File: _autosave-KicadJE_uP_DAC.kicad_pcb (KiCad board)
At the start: 2 copper layers, 100 x 100 mm, 273 parts, among them J201 CV1, J202 CV2, J203 OUT1, J204 OUT2, J205 IN1, J206 IN2, J301 AVR-ISP-6, J302 UART, J401 CV1, J402 CV2, J403 OUT1, J404 OUT2, J405 OUT3, J406 OUT4, J407 IN1, J408 IN2, J409 I2C, J501 BOOT, J502 UART, J503 USB_B_Micro, J601 CV1, J602 FM_lin, J603 Sync, J604 PWM, J605 Ramp, J606 Tri, J607 Sine, J608 555_Pulse, P201 Doepfer_Power_16pin, P401 Doepfer_Power_16pin, P601 Doepfer_Power_16pin, SW201 SW_SPDT, SW401 SW_SPDT, U201 TL072, U202 MCP4822, U301 ATmega32A-AU, U401 TL072, U402 TL072, U405 MCP4822, U501 AMS1117-3.3, U502 STM32F103C8Tx, U601 TLC555, U602 TL074, U603 TL074, Y301 16MHz, Y501 8 MHz

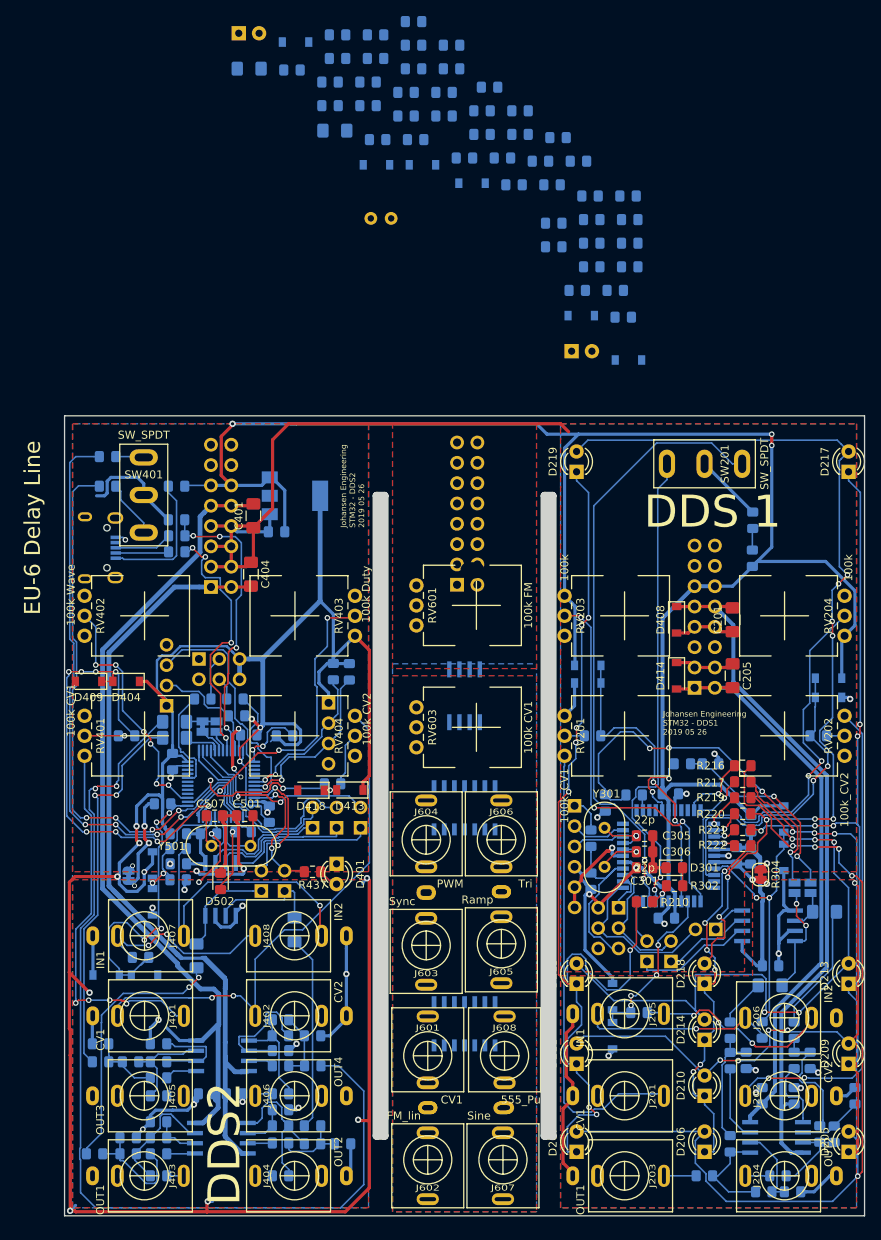
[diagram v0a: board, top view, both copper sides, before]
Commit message: 16p -> 10p on 555 VCO
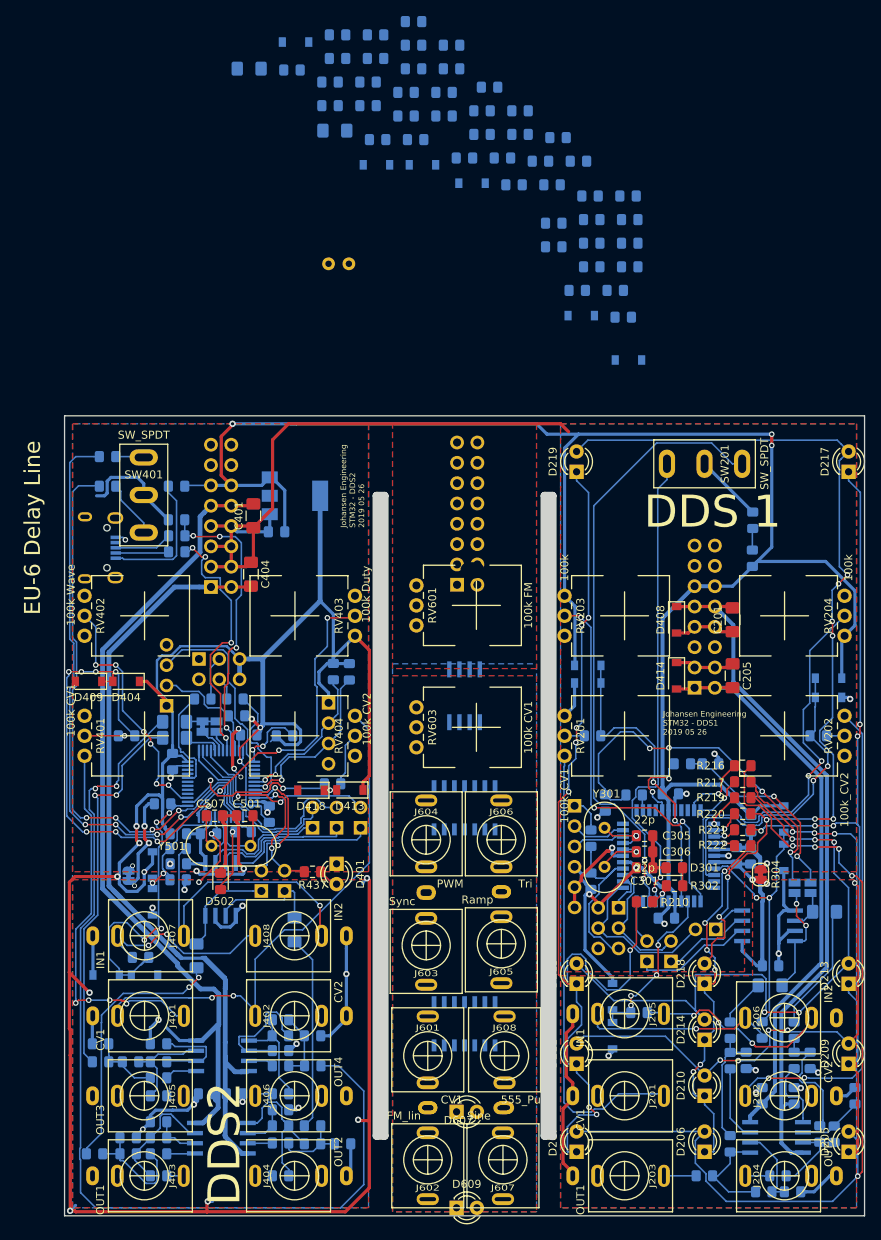
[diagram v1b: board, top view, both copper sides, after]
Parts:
- D607, D609: moved to F.Cu
- moved D609 149.3 mm to (99.0, 149.0)
- moved D607 96.2 mm to (99.0, 137.0)
- moved R607 7.75 mm to (83.0, 31.0)
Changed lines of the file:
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@@
     )
   )
-  (module LED_THT:LED_D3.0mm (layer B.Cu)
-    (at 113.385001 41.924999)
+  (module LED_THT:LED_D3.0mm (layer F.Cu)
+    (at 99 137)
     (descr "LED, diameter 3.0mm, 2 pins")
     (tags "LED diameter 3.0mm 2 pins")
-    (fp_text reference D607 (at 1.27 2.96) (layer B.SilkS)
-      (effects (font (size 1 1) (thickness 0.15)) (justify mirror))
-    )
-    (fp_text value LED (at 1.27 -2.96) (layer B.Fab)
-      (effects (font (size 1 1) (thickness 0.15)) (justify mirror))
-    )
-    (fp_line (start 3.7 2.25) (end -1.15 2.25) (layer B.CrtYd) (width 0.05))
-    (fp_line (start 3.7 -2.25) (end 3.7 2.25) (layer B.CrtYd) (width 0.05))
-    (fp_line (start -1.15 -2.25) (end 3.7 -2.25) (layer B.CrtYd) (width 0.05))
-    (fp_line (start -1.15 2.25) (end -1.15 -2.25) (layer B.CrtYd) (width 0.05))
-    (fp_line (start -0.29 -1.08) (end -0.29 -1.236) (layer B.SilkS) (width 0.12))
-    (fp_line (start -0.29 1.236) (end -0.29 1.08) (layer B.SilkS) (width 0.12))
-    (fp_line (start -0.23 1.16619) (end -0.23 -1.16619) (layer B.Fab) (width 0.1))
-    (fp_circle (center 1.27 0) (end 2.77 0) (layer B.Fab) (width 0.1))
-    (fp_arc (start 1.27 0) (end 0.229039 -1.08) (angle 87.9) (layer B.SilkS) (width 0.12))
-    (fp_arc (start 1.27 0) (end 0.229039 1.08) (angle -87.9) (layer B.SilkS) (width 0.12))
-    (fp_arc (start 1.27 0) (end -0.29 -1.235516) (angle 108.8) (layer B.SilkS) (width 0.12))
-    (fp_arc (start 1.27 0) (end -0.29 1.235516) (angle -108.8) (layer B.SilkS) (width 0.12))
-    (fp_arc (start 1.27 0) (end -0.23 1.16619) (angle -284.3) (layer B.Fab) (width 0.1))
+    (fp_text reference D607 (at 0.229039 1.08) (layer F.SilkS)
+      (effects (font (size 1 1) (thickness 0.15)))
+    )
+    (fp_text value LED (at 1.27 2.96) (layer F.Fab)
+      (effects (font (size 1 1) (thickness 0.15)))
+    )
+    (fp_line (start 3.7 -2.25) (end -1.15 -2.25) (layer F.CrtYd) (width 0.05))
+    (fp_line (start 3.7 2.25) (end 3.7 -2.25) (layer F.CrtYd) (width 0.05))
+    (fp_line (start -1.15 2.25) (end 3.7 2.25) (layer F.CrtYd) (width 0.05))
+    (fp_line (start -1.15 -2.25) (end -1.15 2.25) (layer F.CrtYd) (width 0.05))
+    (fp_line (start -0.29 1.08) (end -0.29 1.236) (layer F.SilkS) (width 0.12))
+    (fp_line (start -0.29 -1.236) (end -0.29 -1.08) (layer F.SilkS) (width 0.12))
+    (fp_line (start -0.23 -1.16619) (end -0.23 1.16619) (layer F.Fab) (width 0.1))
+    (fp_circle (center 1.27 0) (end 2.77 0) (layer F.Fab) (width 0.1))
+    (fp_arc (start 1.27 0) (end 0.229039 1.08) (angle -87.9) (layer F.SilkS) (width 0.12))
+    (fp_arc (start 1.27 0) (end 0.229039 -1.08) (angle 87.9) (layer F.SilkS) (width 0.12))
+    (fp_arc (start 1.27 0) (end -0.29 1.235516) (angle -108.8) (layer F.SilkS) (width 0.12))
+    (fp_arc (start 1.27 0) (end -0.29 -1.235516) (angle 108.8) (layer F.SilkS) (width 0.12))
+    (fp_arc (start 1.27 0) (end -0.23 -1.16619) (angle 284.3) (layer F.Fab) (width 0.1))
     (pad 2 thru_hole circle (at 2.54 0) (size 1.8 1.8) (drill 0.9) (layers *.Cu *.Mask)
       (net 154 "Net-(D607-Pad2)"))
@@
     )
   )
-  (module LED_THT:LED_D3.0mm (layer B.Cu)
-    (at 71.775001 2.184999)
+  (module LED_THT:LED_D3.0mm (layer F.Cu)
+    (at 99 149)
     (descr "LED, diameter 3.0mm, 2 pins")
     (tags "LED diameter 3.0mm 2 pins")
-    (fp_text reference D609 (at 1.27 2.96) (layer B.SilkS)
-      (effects (font (size 1 1) (thickness 0.15)) (justify mirror))
-    )
-    (fp_text value LED (at 1.27 -2.96) (layer B.Fab)
-      (effects (font (size 1 1) (thickness 0.15)) (justify mirror))
-    )
-    (fp_arc (start 1.27 0) (end -0.23 1.16619) (angle -284.3) (layer B.Fab) (width 0.1))
-    (fp_arc (start 1.27 0) (end -0.29 1.235516) (angle -108.8) (layer B.SilkS) (width 0.12))
-    (fp_arc (start 1.27 0) (end -0.29 -1.235516) (angle 108.8) (layer B.SilkS) (width 0.12))
-    (fp_arc (start 1.27 0) (end 0.229039 1.08) (angle -87.9) (layer B.SilkS) (width 0.12))
-    (fp_arc (start 1.27 0) (end 0.229039 -1.08) (angle 87.9) (layer B.SilkS) (width 0.12))
-    (fp_circle (center 1.27 0) (end 2.77 0) (layer B.Fab) (width 0.1))
-    (fp_line (start -0.23 1.16619) (end -0.23 -1.16619) (layer B.Fab) (width 0.1))
-    (fp_line (start -0.29 1.236) (end -0.29 1.08) (layer B.SilkS) (width 0.12))
-    (fp_line (start -0.29 -1.08) (end -0.29 -1.236) (layer B.SilkS) (width 0.12))
-    (fp_line (start -1.15 2.25) (end -1.15 -2.25) (layer B.CrtYd) (width 0.05))
-    (fp_line (start -1.15 -2.25) (end 3.7 -2.25) (layer B.CrtYd) (width 0.05))
-    (fp_line (start 3.7 -2.25) (end 3.7 2.25) (layer B.CrtYd) (width 0.05))
-    (fp_line (start 3.7 2.25) (end -1.15 2.25) (layer B.CrtYd) (width 0.05))
+    (fp_text reference D609 (at 1.27 -2.96) (layer F.SilkS)
+      (effects (font (size 1 1) (thickness 0.15)))
+    )
+    (fp_text value LED (at 1.27 2.96) (layer F.Fab)
+      (effects (font (size 1 1) (thickness 0.15)))
+    )
+    (fp_arc (start 1.27 0) (end -0.23 -1.16619) (angle 284.3) (layer F.Fab) (width 0.1))
+    (fp_arc (start 1.27 0) (end -0.29 -1.235516) (angle 108.8) (layer F.SilkS) (width 0.12))
+    (fp_arc (start 1.27 0) (end -0.29 1.235516) (angle -108.8) (layer F.SilkS) (width 0.12))
+    (fp_arc (start 1.27 0) (end 0.229039 -1.08) (angle 87.9) (layer F.SilkS) (width 0.12))
+    (fp_arc (start 1.27 0) (end 0.229039 1.08) (angle -87.9) (layer F.SilkS) (width 0.12))
+    (fp_circle (center 1.27 0) (end 2.77 0) (layer F.Fab) (width 0.1))
+    (fp_line (start -0.23 -1.16619) (end -0.23 1.16619) (layer F.Fab) (width 0.1))
+    (fp_line (start -0.29 -1.236) (end -0.29 -1.08) (layer F.SilkS) (width 0.12))
+    (fp_line (start -0.29 1.08) (end -0.29 1.236) (layer F.SilkS) (width 0.12))
+    (fp_line (start -1.15 -2.25) (end -1.15 2.25) (layer F.CrtYd) (width 0.05))
+    (fp_line (start -1.15 2.25) (end 3.7 2.25) (layer F.CrtYd) (width 0.05))
+    (fp_line (start 3.7 2.25) (end 3.7 -2.25) (layer F.CrtYd) (width 0.05))
+    (fp_line (start 3.7 -2.25) (end -1.15 -2.25) (layer F.CrtYd) (width 0.05))
     (pad 1 thru_hole rect (at 0 0) (size 1.8 1.8) (drill 0.9) (layers *.Cu *.Mask)
       (net 2 GND))
@@
   )
   (module OptoDevice:R_LDR_4.9x4.2mm_P2.54mm_Vertical (layer B.Cu)
-    (at 88.285001 25.324999)
+    (at 83 31)
     (descr "Resistor, LDR 4.9x4.2mm")
     (tags "Resistor LDR4.9x4.2")
